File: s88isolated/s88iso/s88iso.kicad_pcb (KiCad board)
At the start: 2 copper layers, 70 x 50 mm, 30 parts, among them J1 Barrel_Jack_Switch_MountingPin, J2 5V Bypass, J3 12V 5V, J4 Conn_01x04, U1 L7805, U2 4504, U3 Si8641BB-B

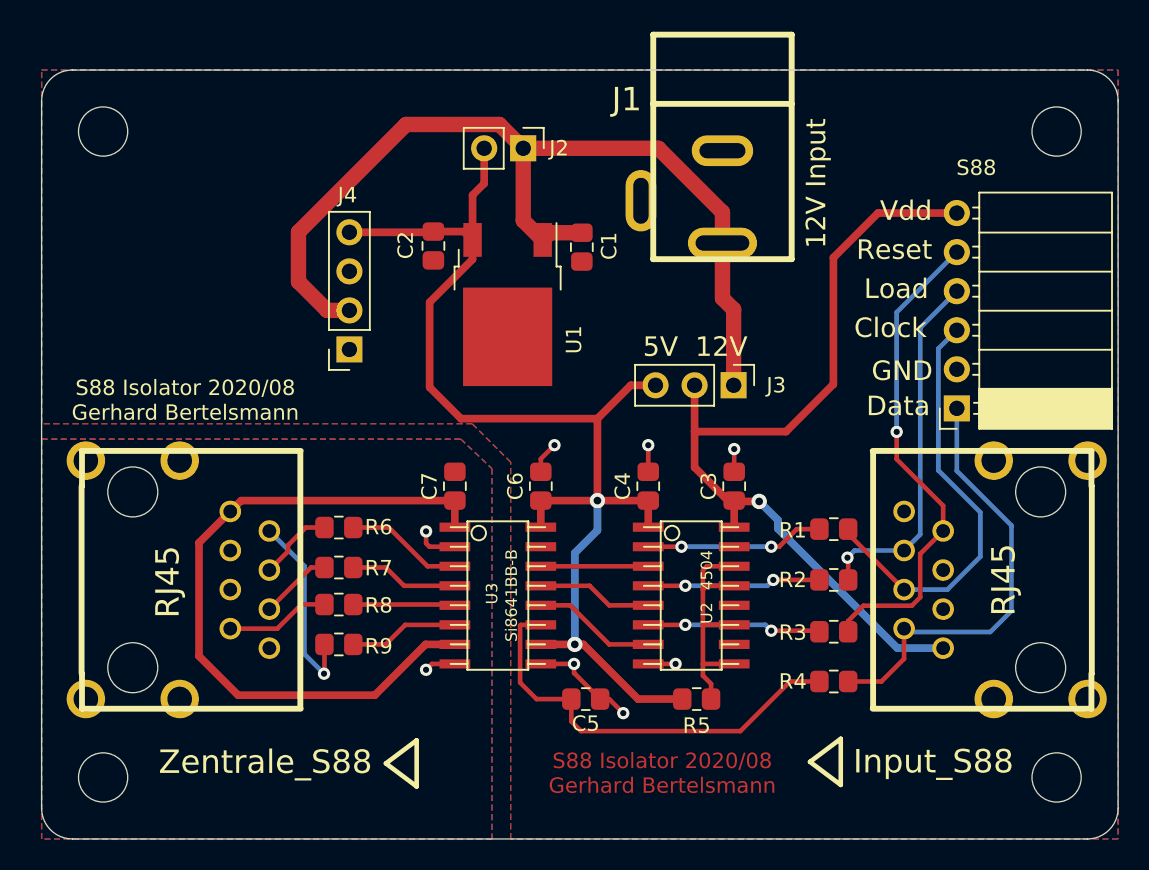
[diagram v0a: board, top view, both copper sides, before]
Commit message: new V2.0 version for JLCPCB Assembly Service
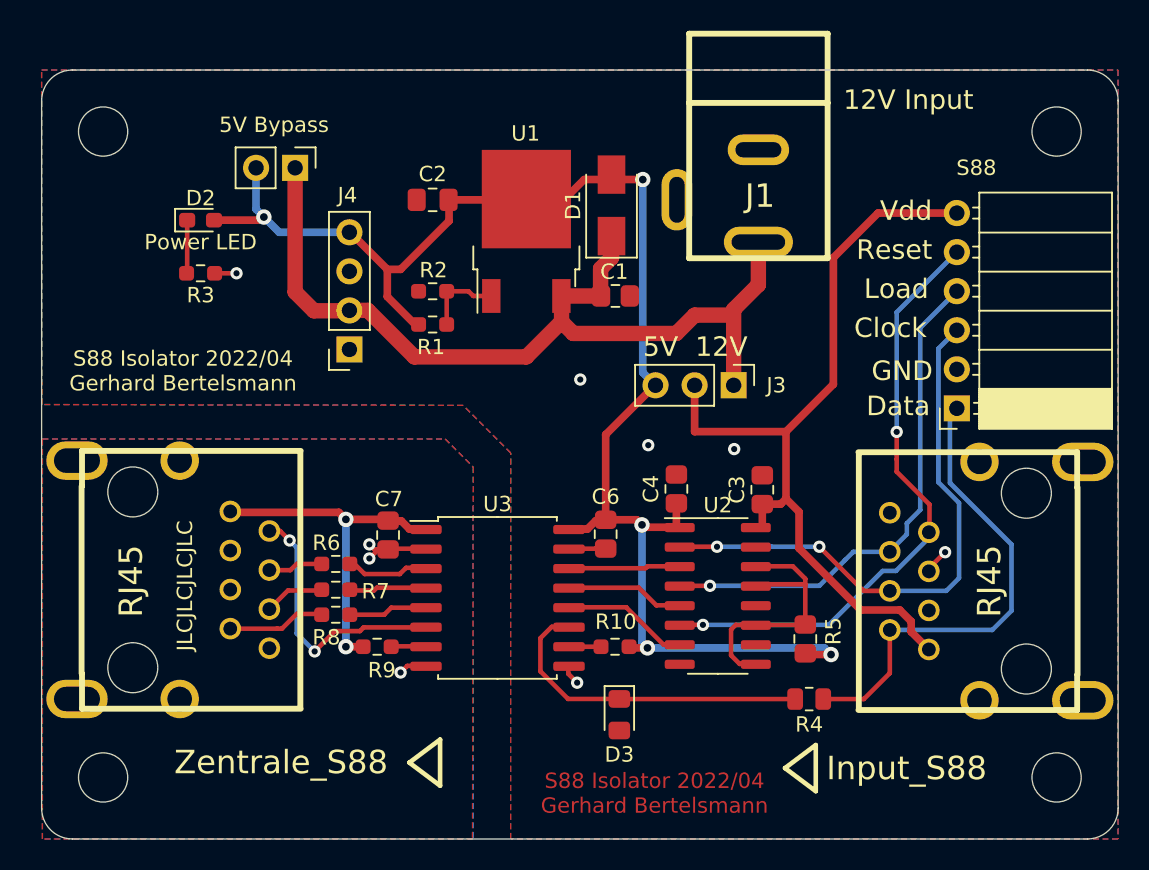
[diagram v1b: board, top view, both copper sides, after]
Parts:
- removed C5: 1nF, Capacitor_SMD:C_0805_2012Metric
- added D1: M7, Diode_SMD:D_SMA, F.Cu at (137.1, 88.8)
- added D2: Power LED, LED_SMD:LED_0603_1608Metric_Pad1.05x0.95mm_HandSolder, F.Cu at (110.3, 89.8)
- added D3: 5V1, Diode_SMD:D_0805_2012Metric_Pad1.15x1.40mm_HandSolder, F.Cu at (137.6, 121.9)
- added R10: 1k, Resistor_SMD:R_0603_1608Metric_Pad0.98x0.95mm_HandSolder, F.Cu at (137.3, 117.5)
- C2: value 100nF -> 1uF; footprint Capacitor_SMD:C_0805_2012Metric -> Capacitor_SMD:C_0805_2012Metric_Pad1.18x1.45mm_HandSolder
- R1: value 47 -> 240; footprint Resistor_SMD:R_0805_2012Metric -> Resistor_SMD:R_0603_1608Metric_Pad0.98x0.95mm_HandSolder
- R2: value 47 -> 750; footprint Resistor_SMD:R_0805_2012Metric -> Resistor_SMD:R_0603_1608Metric_Pad0.98x0.95mm_HandSolder
- R3: value 47 -> 270; footprint Resistor_SMD:R_0805_2012Metric -> Resistor_SMD:R_0603_1608Metric_Pad0.98x0.95mm_HandSolder
- R6, R7, R8: value 47 -> 56; footprint Resistor_SMD:R_0805_2012Metric -> Resistor_SMD:R_0603_1608Metric_Pad0.98x0.95mm_HandSolder
- R9: value 47 -> 1k; footprint Resistor_SMD:R_0805_2012Metric -> Resistor_SMD:R_0603_1608Metric_Pad0.98x0.95mm_HandSolder
- U1: value L7805 -> LM317
- U2: footprint w_smd_dil:so-16 -> Package_SO:SOIC-16_3.9x9.9mm_P1.27mm
- U3: value Si8641BB-B -> NSI8141W1; footprint w_smd_dil:so-16 -> Package_SO:SOIC-16W_7.5x10.3mm_P1.27mm
- moved R3 47.3 mm to (110.3, 93.2), turned to 0 degrees
- moved R2 32.1 mm to (125.4, 94.4)
- moved R1 29.3 mm to (125.4, 96.5), turned to 0 degrees
- moved J2 14.9 mm to (116.5, 86.4)
- moved R5 8.07 mm to (149.7, 117.0), turned to 90 degrees
- moved C7 5.38 mm to (122.5, 110.2), turned to 270 degrees
- moved C6 5.25 mm to (136.7, 110.2), turned to 270 degrees
- moved U1 4.91 mm to (131.5, 90.5), turned to 90 degrees
- moved C1 3.85 mm to (137.3, 94.7), turned to 0 degrees
- moved C2 3.00 mm to (125.4, 88.4), turned to 180 degrees
- moved R9 2.49 mm to (121.8, 117.5)
- moved R6 2.38 mm to (119.1, 112.1)
- moved J1 2.34 mm to (146.6, 84.9)
- moved R4 1.97 mm to (149.9, 120.9)
- moved C3 1.84 mm to (146.9, 107.3)
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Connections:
- R1 pad 1: /Clock' -> +5VD
- R2 pad 1: /PSLoad' -> Net-(R1-Pad2)
- R2 pad 2: Net-(R2-Pad2) -> GNDD
- R3 pad 1: /Reset' -> Net-(D2-Pad1)
- R3 pad 2: Net-(R3-Pad2) -> GNDD
- R9 pad 2: /Data -> +5V
- U1 pad 1: /Input -> Net-(R1-Pad2)
- U1 pad 2: GNDD -> +5VD
- U1 pad 3: +5VD -> /Input
- U2 pad 2: Net-(R1-Pad2) -> /Clock'
- U2 pad 4: Net-(R2-Pad2) -> /PSLoad'
- U2 pad 6: Net-(R3-Pad2) -> /Reset'
- U3 pad 10: +5VD -> Net-(R10-Pad2)
- U3 pad 6: Net-(R9-Pad1) -> /Data
- U3 pad 7: +5V -> Net-(R9-Pad1)
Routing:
- net +5V: track 45.9 -> 22.2 mm, vias 0 -> 2
- net +5VD: track 78.1 -> 96.6 mm, vias 2 -> 5
- net Net-(R3-Pad2): track 11.3 -> 0.00 mm, vias 2 -> 0
- net Net-(R2-Pad2): track 11.3 -> 0.00 mm, vias 2 -> 0
- net /PSLoad': track 23.6 -> 33.5 mm
- net /Clock': track 27.6 -> 37.1 mm, vias 0 -> 2
- net /Reset': track 32.0 -> 39.8 mm, vias 1 -> 2
- net GNDD: track 14.1 -> 6.31 mm
- net Net-(D3-Pad1): track 28.0 -> 21.6 mm
- net Net-(R1-Pad2): track 11.6 -> 5.21 mm, vias 2 -> 0
- net Net-(R9-Pad1): track 7.13 -> 1.91 mm
- net /Data: track 12.7 -> 17.0 mm, vias 1 -> 2
- net Net-(D2-Pad1): track 0.00 -> 3.47 mm
- net /Data': track 28.5 -> 31.3 mm
- net VDD: track 56.2 -> 53.4 mm, vias 1 -> 0
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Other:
- board text added: "JLCJLCJLCJLC"
- board text added: "S88 Isolator 2022/04 Gerhard Bertelsmann"
- board text removed: "S88 Isolator 2020/08 Gerhard Bertelsmann"
